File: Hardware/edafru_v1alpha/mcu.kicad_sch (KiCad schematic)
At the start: 34 parts, among them J2 ICSP, U5 PIC18F25K80_ISS, U7 AT24CS02-SSHM, Y1 8.000 MHz

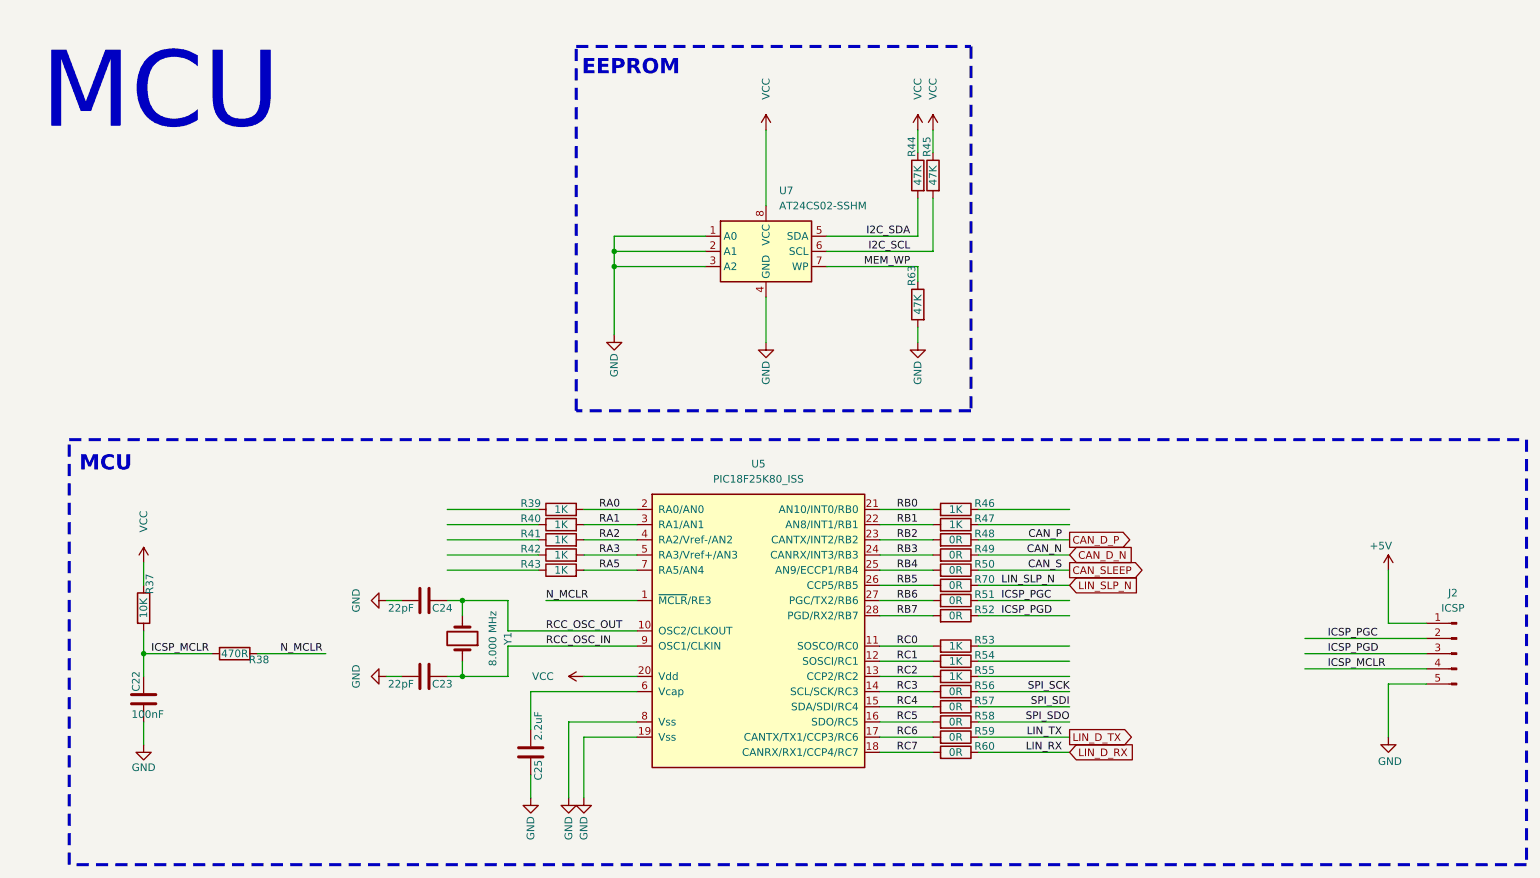
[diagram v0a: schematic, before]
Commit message: all need circuits included to the schematic. ready for pcb component placement.
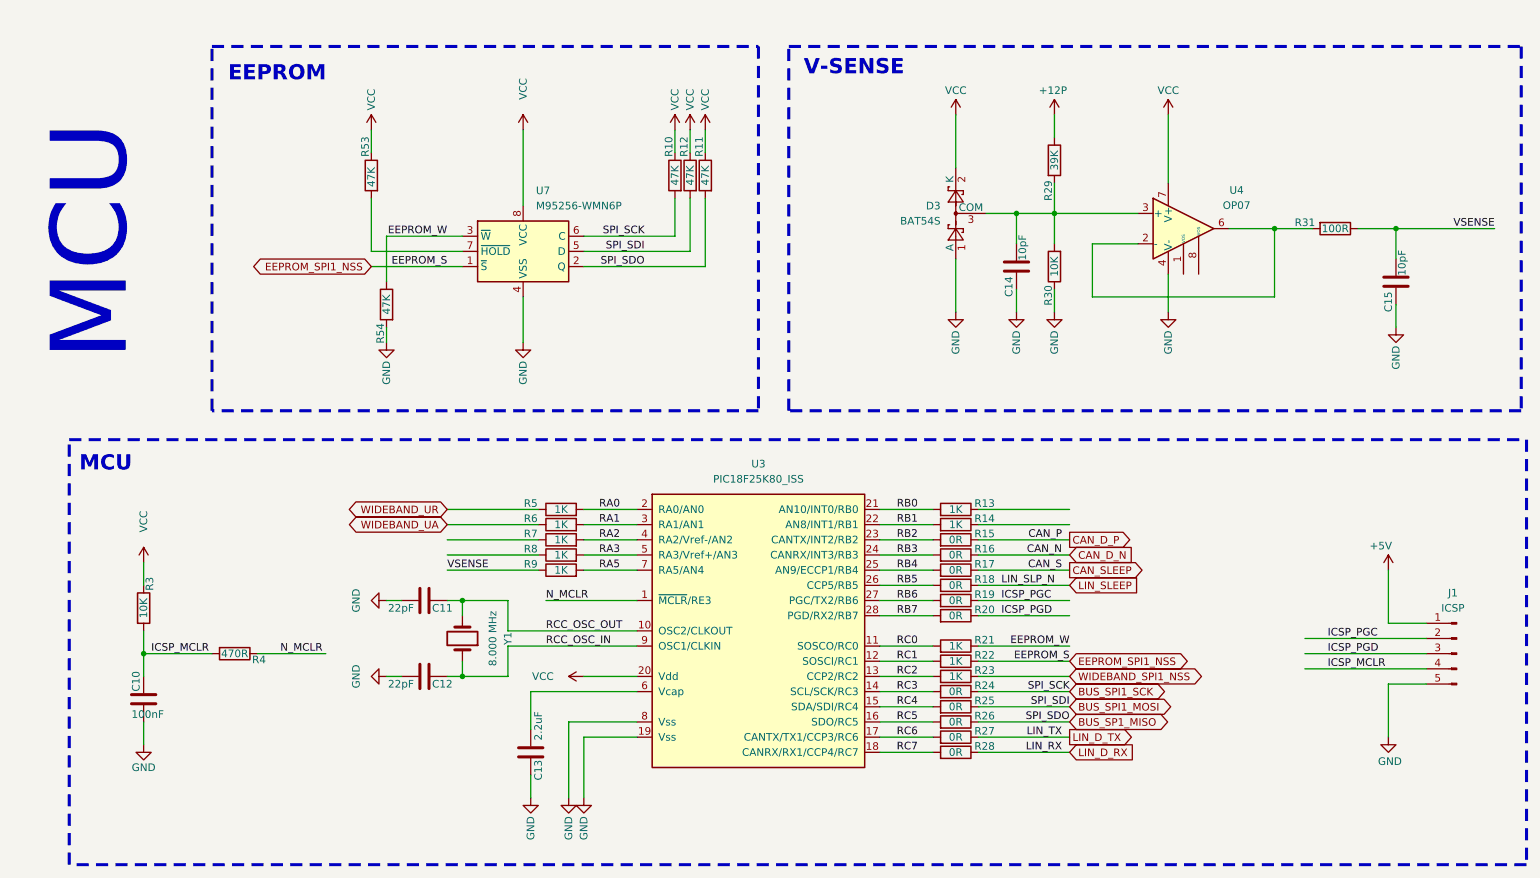
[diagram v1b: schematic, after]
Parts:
- removed U7: AT24CS02-SSHM, Package_SO:SOIC-8_3.9x4.9mm_P1.27mm, symbol Memory_EEPROM:AT24CS02-SSHM
- added C14, C15: 10pF, Capacitor_SMD:C_0603_1608Metric_Pad1.08x0.95mm_HandSolder, symbol Device:C
- added D3: BAT54S, Package_TO_SOT_SMD:SOT-23, symbol Diode:BAT54S
- added R29: 39K, Resistor_SMD:R_0603_1608Metric_Pad0.98x0.95mm_HandSolder, symbol Device:R
- added R30: 10K, Resistor_SMD:R_0603_1608Metric_Pad0.98x0.95mm_HandSolder, symbol Device:R
- added R31: 100R, Resistor_SMD:R_0603_1608Metric_Pad0.98x0.95mm_HandSolder, symbol Device:R
- added R53, R54: 47K, Resistor_SMD:R_0603_1608Metric_Pad0.98x0.95mm_HandSolder, symbol Device:R
- added U4: OP07, Package_SO:SOIC-8_3.9x4.9mm_P1.27mm, symbol Amplifier_Operational:OP07
- added U7: M95256-WMN6P, Package_DFN_QFN:WFDFPN-8-1EP_3x2mm_P0.5mm_EP1.25x1.35mm, symbol Memory_EEPROM:M95256-WMN6P
- renumbered C22 to C10, C24 to C11, C23 to C12, C25 to C13, J2 to J1, R44 to R10, R63 to R11, R45 to R12, R46 to R13, R47 to R14, R48 to R15, R49 to R16, R50 to R17, R70 to R18, R51 to R19, R52 to R20, R53 to R21, R54 to R22, R55 to R23, R56 to R24, R57 to R25, R58 to R26, R59 to R27, R60 to R28, R37 to R3, R38 to R4, R39 to R5, R40 to R6, R41 to R7, R42 to R8, R43 to R9, U5 to U3
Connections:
- net MEM_WP is gone; now on net VCC: R11.1
- net SPI_SCK is gone; now on net BUS_SPI1_SCK: R24.1
- net SPI_SDI is gone; now on net BUS_SPI1_MOSI: R25.1
- net GND: now also C14.2, C15.2, D3.1 (A), R30.1, R54.2, U4.4 (V-), U7.4 (VSS); no longer R11.2
- net VCC: now also D3.2 (K), R53.1, U4.7 (V+), U7.8 (VCC)
- net WIDEBAND_UR: now reaches R5.1
- net EEPROM_SPI1_NSS: now reaches R22.1
- net EEPROM_SPI1_NSS: now also U7.1 (~{S})
- net WIDEBAND_UA: now reaches R6.1
- net WIDEBAND_SPI1_NSS: now reaches R23.1
- net EEPROM_W: now reaches R21.1
- net EEPROM_W: now also R54.1, U7.3 (~{W})
- net VSENSE: now reaches R9.1
- net VSENSE: now also C15.1, R31.1
- net I2C_SCL renamed BUS_SPI1_MOSI
- net BUS_SPI1_MOSI: now also U7.5 (D)
- net I2C_SDA renamed BUS_SPI1_SCK
- net BUS_SPI1_SCK: now also U7.6 (C)
- net LIN_SLP_N renamed LIN_SLEEP
- net SPI_SDO renamed BUS_SP1_MISO
- net BUS_SP1_MISO: now also R11.2, U7.2 (Q)
- new net: C14.1, D3.3 (COM), R29.2, R30.2, U4.3 (+)
- new net: R31.2, U4.2 (-), U4.6
- new net: R53.2, U7.7 (~{HOLD})
- new net +12P: R29.1
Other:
- note added: "V-SENSE"
- moved on the sheet: R10, R11, R12

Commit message: PCB is developing...
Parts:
- removed R13, R14, R21, R22, R5, R6: 1K, Resistor_SMD:R_0603_1608Metric_Pad0.98x0.95mm_HandSolder, symbol Device:R
- removed U7: M95256-WMN6P, Package_DFN_QFN:WFDFPN-8-1EP_3x2mm_P0.5mm_EP1.25x1.35mm, symbol Memory_EEPROM:M95256-WMN6P
- added R10, R11, R15, R16, R24, R25: 0R, Resistor_SMD:R_0603_1608Metric_Pad0.98x0.95mm_HandSolder, symbol Device:R
- added U2: M95256-WMN6P, Package_SO:SOIC-8_3.9x4.9mm_P1.27mm, symbol Memory_EEPROM:M95256-WMN6P
- R23, R7, R8, R9: value 1K -> 0R
- renumbered J1 to J3, R10 to R12, R12 to R13, R11 to R14, R15 to R17, R16 to R18, R17 to R19, R18 to R20, R19 to R21, R20 to R22, R24 to R26, R25 to R27, R26 to R28, R27 to R29, R28 to R30, R29 to R31, R30 to R32, R31 to R33, R53 to R5, R54 to R6
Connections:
- net BUS_SP1_MISO: now also U2.2 (Q)
- net BUS_SPI1_MOSI: now also U2.5 (D)
- net BUS_SPI1_SCK: now also U2.6 (C)
- net EEPROM_SPI1_NSS: now also R24.1, U2.1 (~{S})
- net EEPROM_W: now also R23.1, U2.3 (~{W})
- net GND: now also U2.4 (VSS)
- net RA0: now also R7.1
- net RA1: now also R8.1
- net RA2: now also R9.1; no longer R7.2
- net RA3: now also R10.1; no longer R8.2
- net RA5: now also R11.1; no longer R9.2
- net RB0: now also R15.2
- net RB1: now also R16.2
- net RC0: now also R23.2
- net RC1: now also R24.2
- net RC2: now also R25.2; no longer R23.2
- net VCC: now also U2.8 (VCC)
- net VSENSE: now also R15.1; no longer R9.1
- net WIDEBAND_SPI1_NSS: now also R25.1; no longer R23.1
- net WIDEBAND_UA: now also R8.2
- net WIDEBAND_UR: now also R7.2
- net at R5.2: now also U2.7 (~{HOLD})
- net ICSP_PGC renamed COM_TX
- net ICSP_PGD renamed COM_RX
- new net WIDEBAND_DIAHD: R11.2
- new net WIDEBAND_DIAHG: R10.2
- new net WIDEBAND_RST: R9.2

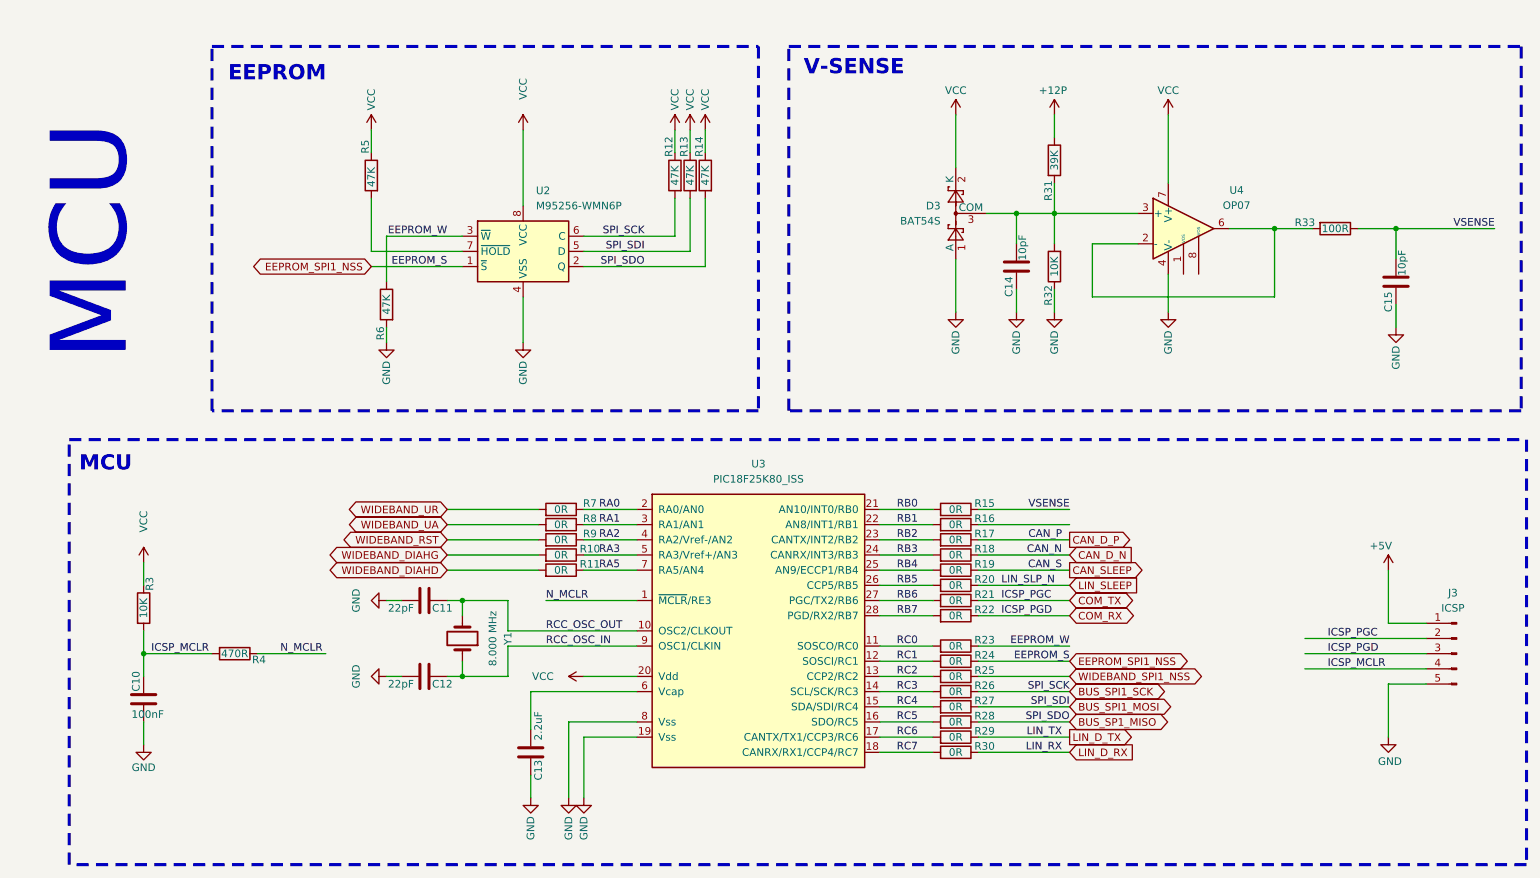
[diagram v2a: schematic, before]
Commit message: developement is stopped depend on new EDVDU.
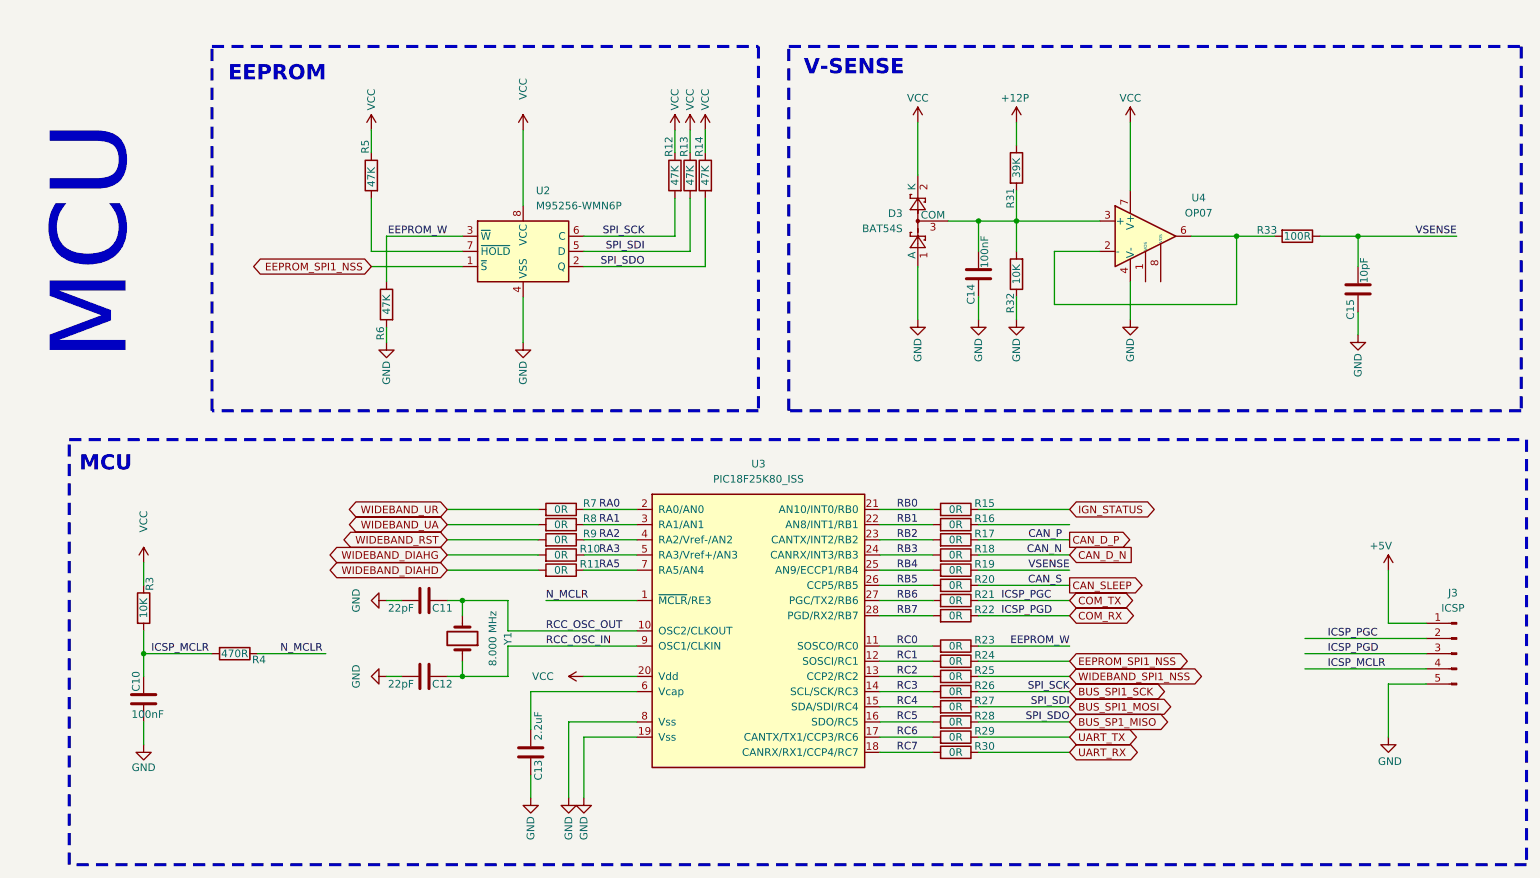
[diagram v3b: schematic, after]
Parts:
- C14: value 10pF -> 100nF
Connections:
- net LIN_SLEEP is gone; now on net CAN_SLEEP: R20.1
- net CAN_SLEEP: no longer R19.1
- net VSENSE: now also R19.1; no longer R15.1
- net LIN_D_RX renamed UART_RX
- net LIN_D_TX renamed UART_TX
- new net IGN_STATUS: R15.1
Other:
- moved on the sheet: C14, C15, D3, R31, R32, R33, U4
